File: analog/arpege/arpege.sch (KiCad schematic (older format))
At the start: 43 parts, among them J1 Conn_01x02, J2 Conn_01x02, J3 Conn_01x06, J4 AudioJack3, SW1 SW_SPDT, SW2 SW_SPDT, U1 TL062, U2 TL062

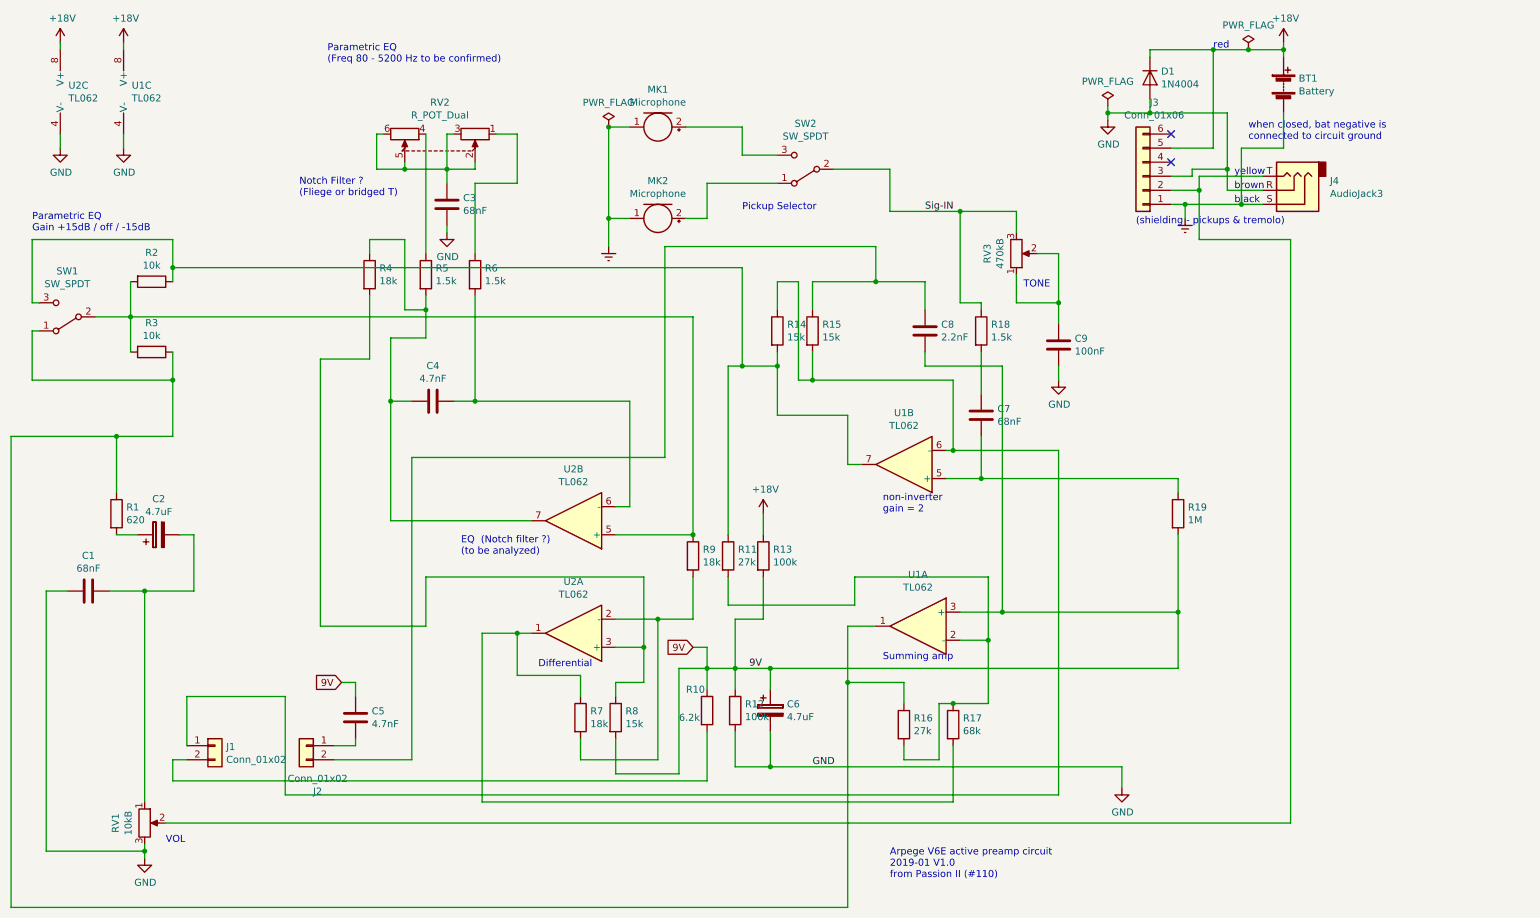
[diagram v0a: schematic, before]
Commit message: added some components values, clean up edge connector
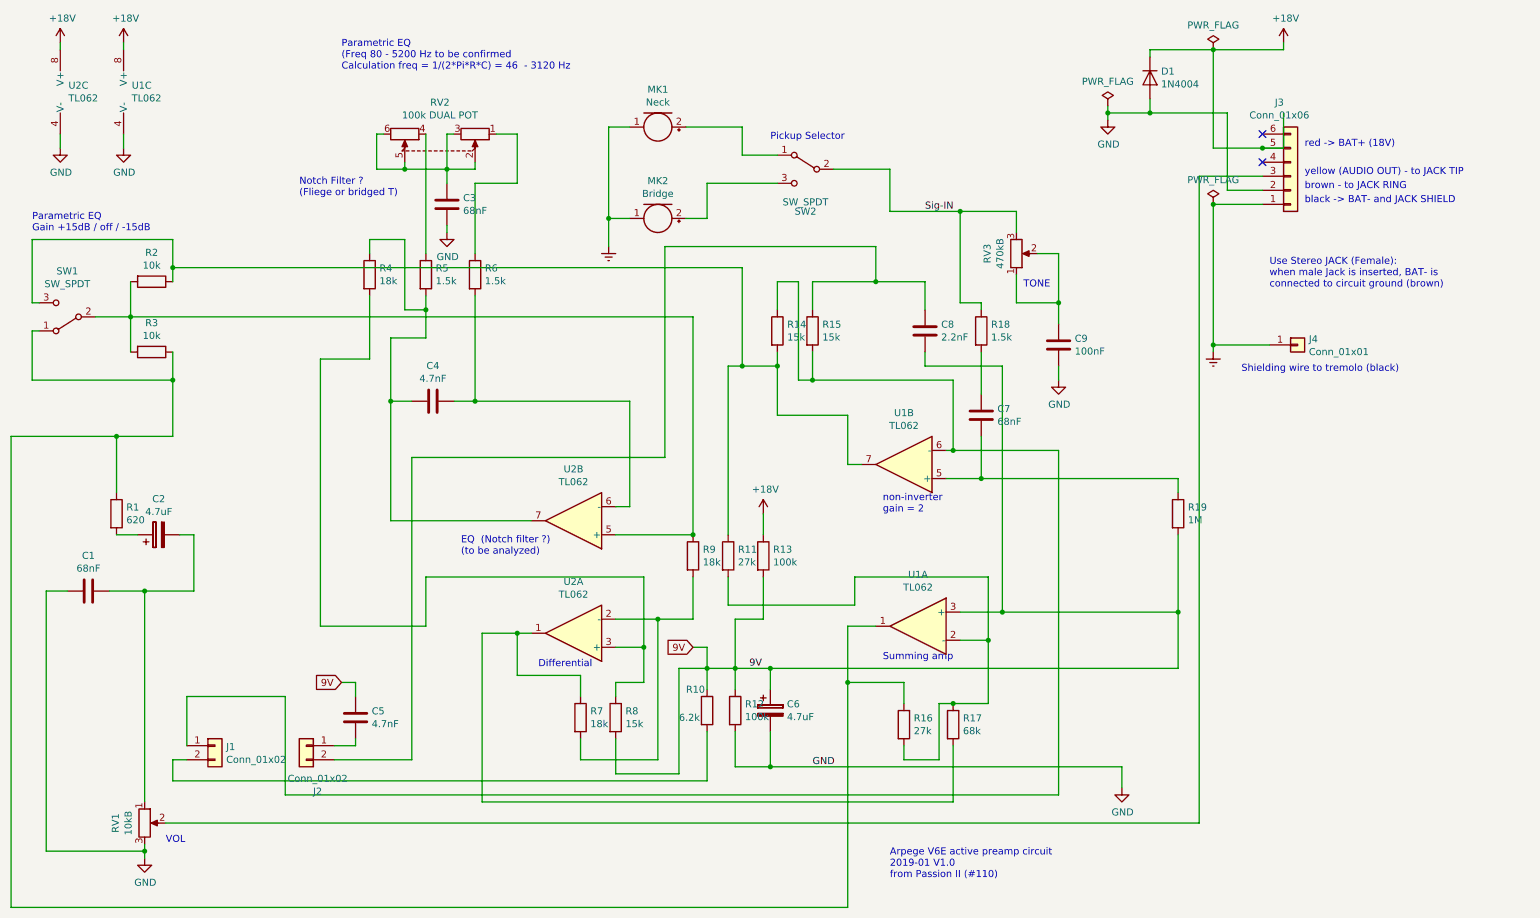
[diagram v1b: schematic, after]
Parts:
- removed BT1: Battery, symbol Device:Battery
- removed J4: AudioJack3, symbol Connector:AudioJack3
- added J4: Conn_01x01, symbol Connector_Generic:Conn_01x01
- MK1: value Microphone -> Neck
- MK2: value Microphone -> Bridge
- RV2: value R_POT_Dual -> 100k DUAL POT
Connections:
- net Earth: now also J4.1 (Pin_1)
- net GND: now also J3.2 (Pin_2); no longer J3.3 (Pin_3)
- net at RV1.2: now also J3.3 (Pin_3); no longer J3.2 (Pin_2)
- net at SW2.1 (A): now also MK1.2 (+); no longer MK2.2 (+)
- net at SW2.3 (C): now also MK2.2 (+); no longer MK1.2 (+)
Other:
- note added: "Parametric EQ \n(Freq 80 - 5200 Hz to be confirmed\nCalculation freq = 1/(2*Pi*R*C) = 46 - 3120 Hz"
- note added: "Shielding wire to tremolo (black)"
- note added: "Use Stereo JACK (Female): \nwhen male Jack is inserted, BAT- is \nconnected to circuit ground (brown)"
- note added: "black -> BAT- and JACK SHIELD"
- note added: "brown - to JACK RING"
- note added: "red -> BAT+ (18V)"
- note added: "yellow (AUDIO OUT) - to JACK TIP"
- note removed: "(shielding - pickups & tremolo)"
- note removed: "Parametric EQ \n(Freq 80 - 5200 Hz to be confirmed)"
- note removed: "black"
- note removed: "brown"
- note removed: "red"
- note removed: "when closed, bat negative is \nconnected to circuit ground"
- note removed: "yellow"
- moved on the sheet: J3
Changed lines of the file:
@@
 Arpege V6E active preamp circuit\n2019-01 V1.0\nfrom Passion II (#110)\n
-$Comp
-L Device:Battery BT1
-U 1 1 5C31AA7D
-P 9800 1150
-F 0 "BT1" H 9908 1196 50  0000 L CNN
-F 1 "Battery" H 9908 1105 50  0000 L CNN
-F 2 "" V 9800 1210 50  0001 C CNN
-F 3 "~" V 9800 1210 50  0001 C CNN
-	1    9800 1150
-	1    0    0    -1
-$EndComp
 $Comp
 L Device:R_POT RV3
@@
 	0    1    1    0
 $EndComp
-Wire Wire Line
-	9800 950  9800 900
 $Comp
 L arpege-rescue:+18V-power #PWR012
@@
 U 1 1 5C31D5B5
 P 6400 1750
-F 0 "SW2" H 6400 1425 50  0000 C CNN
+F 0 "SW2" H 6400 1450 50  0000 C CNN
 F 1 "SW_SPDT" H 6400 1516 50  0000 C CNN
 F 2 "" H 6400 1750 50  0001 C CNN
 F 3 "" H 6400 1750 50  0001 C CNN
 	1    6400 1750
-	-1   0    0    1
+	-1   0    0    -1
 $EndComp
 $Comp
@@
 P 3800 1600
 F 0 "RV2" H 3800 1275 50  0000 C CNN
-F 1 "R_POT_Dual" H 3800 1366 50  0000 C CNN
+F 1 "100k DUAL POT" H 3800 1366 50  0000 C CNN
 F 2 "" H 4050 1525 50  0001 C CNN
 F 3 "~" H 4050 1525 50  0001 C CNN
@@
 P 5350 1450
 F 0 "MK1" V 5083 1450 50  0000 C CNN
-F 1 "Microphone" V 5174 1450 50  0000 C CNN
+F 1 "Neck" V 5174 1450 50  0000 C CNN
 F 2 "" V 5350 1550 50  0001 C CNN
 F 3 "~" V 5350 1550 50  0001 C CNN
@@
 P 5350 2100
 F 0 "MK2" V 5083 2100 50  0000 C CNN
-F 1 "Microphone" V 5174 2100 50  0000 C CNN
+F 1 "Bridge" V 5174 2100 50  0000 C CNN
 F 2 "" V 5350 2200 50  0001 C CNN
 F 3 "~" V 5350 2200 50  0001 C CNN
 	1    5350 2100
 	0    1    1    0
-$EndComp
-$Comp
-L Connector:AudioJack3 J4
-U 1 1 5C31E95E
-P 9850 1900
-F 0 "J4" H 9570 1833 50  0000 R CNN
-F 1 "AudioJack3" H 9570 1924 50  0000 R CNN
-F 2 "" H 9850 1900 50  0001 C CNN
-F 3 "~" H 9850 1900 50  0001 C CNN
-	1    9850 1900
-	-1   0    0    1
 $EndComp
 $Comp
@@
 	1    0    0    -1
 $EndComp
-Text Notes 9450 1900 0    50   ~ 0
-brown
-Text Notes 9450 2000 0    50   ~ 0
-black
-Text Notes 9450 1800 0    50   ~ 0
-yellow
+Text Notes 9950 1900 0    50   ~ 0
+brown - to JACK RING
+Text Notes 9950 2000 0    50   ~ 0
+black -> BAT- and JACK SHIELD
+Text Notes 9950 1800 0    50   ~ 0
+yellow (AUDIO OUT) - to JACK TIP
 Wire Wire Line
 	9800 1350 9800 1600
 Wire Wire Line
-	9800 1600 9500 1600
-Wire Wire Line
-	9500 1600 9500 2000
-Wire Wire Line
-	9200 1800 9200 1900
+	9800 1600 9650 1600
 Wire Wire Line
 	9650 1900 9400 1900
-Wire Wire Line
-	9400 1750 9150 1750
-Wire Wire Line
-	9150 1750 9150 1800
-Wire Wire Line
-	9150 1800 9000 1800
 Wire Wire Line
 	9400 1350 8850 1350
@@
 L power:Earth #PWR011
 U 1 1 5C3212CD
-P 9100 2100
-F 0 "#PWR011" H 9100 1850 50  0001 C CNN
-F 1 "Earth" H 9100 1950 50  0001 C CNN
-F 2 "" H 9100 2100 50  0001 C CNN
-F 3 "~" H 9100 2100 50  0001 C CNN
-	1    9100 2100
-	1    0    0    -1
-$EndComp
-Wire Wire Line
-	9000 2000 9100 2000
-Wire Wire Line
-	9100 2000 9100 2100
-Text Notes 8750 2150 0    50   ~ 0
-(shielding - pickups & tremolo)
-Connection ~ 9100 2000
+P 9300 3050
+F 0 "#PWR011" H 9300 2800 50  0001 C CNN
+F 1 "Earth" H 9300 2900 50  0001 C CNN
+F 2 "" H 9300 3050 50  0001 C CNN
+F 3 "~" H 9300 3050 50  0001 C CNN
+	1    9300 3050
+	1    0    0    -1
+$EndComp
+Text Notes 9500 3200 0    50   ~ 0
+Shielding wire to tremolo (black)
 $Comp
 L power:GND #PWR09
@@
 	1550 1500 1550 1600
 Wire Wire Line
-	9800 900  9550 900
-Connection ~ 9800 900
-Wire Wire Line
 	9800 900  9800 850
-Text Notes 9300 900  0    50   ~ 0
-red
+Text Notes 9950 1600 0    50   ~ 0
+red -> BAT+ (18V)
 $Comp
 L power:PWR_FLAG #FLG02
 U 1 1 5C342F20
-P 9550 900
-F 0 "#FLG02" H 9550 975 50  0001 C CNN
-F 1 "PWR_FLAG" H 9550 1074 50  0000 C CNN
-F 2 "" H 9550 900 50  0001 C CNN
-F 3 "~" H 9550 900 50  0001 C CNN
-	1    9550 900
-	1    0    0    -1
-$EndComp
-Connection ~ 9550 900
-Wire Wire Line
-	9550 900  9300 900
+P 9300 900
+F 0 "#FLG02" H 9300 975 50  0001 C CNN
+F 1 "PWR_FLAG" H 9300 1074 50  0000 C CNN
+F 2 "" H 9300 900 50  0001 C CNN
+F 3 "~" H 9300 900 50  0001 C CNN
+	1    9300 900
+	1    0    0    -1
+$EndComp
 $Comp
 L power:PWR_FLAG #FLG01
@@
 L Connector_Generic:Conn_01x06 J3
 U 1 1 5C469EF8
-P 8800 1800
-F 0 "J3" H 8720 1275 50  0000 C CNN
-F 1 "Conn_01x06" H 8720 1366 50  0000 C CNN
-F 2 "" H 8800 1800 50  0001 C CNN
-F 3 "~" H 8800 1800 50  0001 C CNN
-	1    8800 1800
-	-1   0    0    1
+P 9850 1800
+F 0 "J3" H 9770 1275 50  0000 C CNN
+F 1 "Conn_01x06" H 9770 1366 50  0000 C CNN
+F 2 "" H 9850 1800 50  0001 C CNN
+F 3 "~" H 9850 1800 50  0001 C CNN
+	1    9850 1800
+	1    0    0    1
 $EndComp
 Wire Wire Line
 	9300 900  9300 1600
-Wire Wire Line
-	9300 1600 9000 1600
 Wire Wire Line
 	3600 3400 3450 3400
@@
 Wire Wire Line
 	1650 4350 1500 4350
-NoConn ~ 9000 1700
-NoConn ~ 9000 1500
+NoConn ~ 9650 1700
+NoConn ~ 9650 1500
 $Comp
 L Amplifier_Operational:TL062 U1
@@
 Sig-IN
 Wire Wire Line
-	9000 1900 9200 1900
-Wire Wire Line
 	1700 6650 1700 6600
 Wire Wire Line
@@
 L power:PWR_FLAG #FLG0101
 U 1 1 5CAD682B
-P 5000 1450
-F 0 "#FLG0101" H 5000 1525 50  0001 C CNN
-F 1 "PWR_FLAG" H 5000 1624 50  0000 C CNN
-F 2 "" H 5000 1450 50  0001 C CNN
-F 3 "~" H 5000 1450 50  0001 C CNN
-	1    5000 1450
-	1    0    0    -1
-$EndComp
-Connection ~ 5000 1450
-Text Notes 9550 1550 0    50   ~ 0
-when closed, bat negative is \nconnected to circuit ground
-Text Notes 3000 1000 0    50   ~ 0
-Parametric EQ \n(Freq 80 - 5200 Hz to be confirmed)
+P 9300 2000
+F 0 "#FLG0101" H 9300 2075 50  0001 C CNN
+F 1 "PWR_FLAG" H 9300 2174 50  0000 C CNN
+F 2 "" H 9300 2000 50  0001 C CNN
+F 3 "~" H 9300 2000 50  0001 C CNN
+	1    9300 2000
+	1    0    0    -1
+$EndComp
+Text Notes 9700 2600 0    50   ~ 0
+Use Stereo JACK (Female): \nwhen male Jack is inserted, BAT- is \nconnected to circuit ground (brown)
+Text Notes 3100 1050 0    50   ~ 0
+Parametric EQ \n(Freq 80 - 5200 Hz to be confirmed\nCalculation freq = 1/(2*Pi*R*C) = 46  - 3120 Hz
 Text Notes 900  2200 0    50   ~ 0
 Parametric EQ\nGain +15dB / off / -15dB
@@
 	1700 4750 2050 4750
 Wire Wire Line
-	9850 2250 9200 2250
-Wire Wire Line
-	9200 2250 9200 1900
-Connection ~ 9200 1900
-Wire Wire Line
 	1150 4750 1000 4750
 Wire Wire Line
@@
 Wire Wire Line
 	1700 6600 1700 6550
-Wire Wire Line
-	9100 2000 9500 2000
-Wire Wire Line
-	9400 1750 9400 1350
-Wire Wire Line
-	9400 1900 9400 1750
-Connection ~ 9400 1750
-Connection ~ 9500 2000
-Wire Wire Line
-	9500 2000 9650 2000
 Connection ~ 8550 1350
 Wire Wire Line
 	8550 1350 8550 1400
 Wire Wire Line
-	1850 6400 9850 6400
-Wire Wire Line
-	9850 2250 9850 6400
-Text Notes 5950 2050 0    50   ~ 0
+	1850 6400 9200 6400
+Text Notes 6150 1550 0    50   ~ 0
 Pickup Selector
+Wire Wire Line
+	9650 1600 9300 1600
+Connection ~ 9650 1600
+Wire Wire Line
+	9400 1350 9400 1900
+Wire Wire Line
+	9200 1800 9200 6400
+$Comp
+L Connector_Generic:Conn_01x01 J4
+U 1 1 5C5212B1
+P 9900 3000
+F 0 "J4" H 9980 3042 50  0000 L CNN
+F 1 "Conn_01x01" H 9980 2951 50  0000 L CNN
+F 2 "" H 9900 3000 50  0001 C CNN
+F 3 "~" H 9900 3000 50  0001 C CNN
+	1    9900 3000
+	1    0    0    -1
+$EndComp
+Wire Wire Line
+	9300 900  9800 900
+Wire Wire Line
+	9300 2000 9650 2000
+Wire Wire Line
+	9700 3000 9300 3000
+Wire Wire Line
+	9300 3000 9300 2000
+Connection ~ 9300 2000
+Wire Wire Line
+	9300 3050 9300 3000
+Connection ~ 9300 3000
 $EndSCHEMATC

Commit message: added notes / labels to booster switch signals
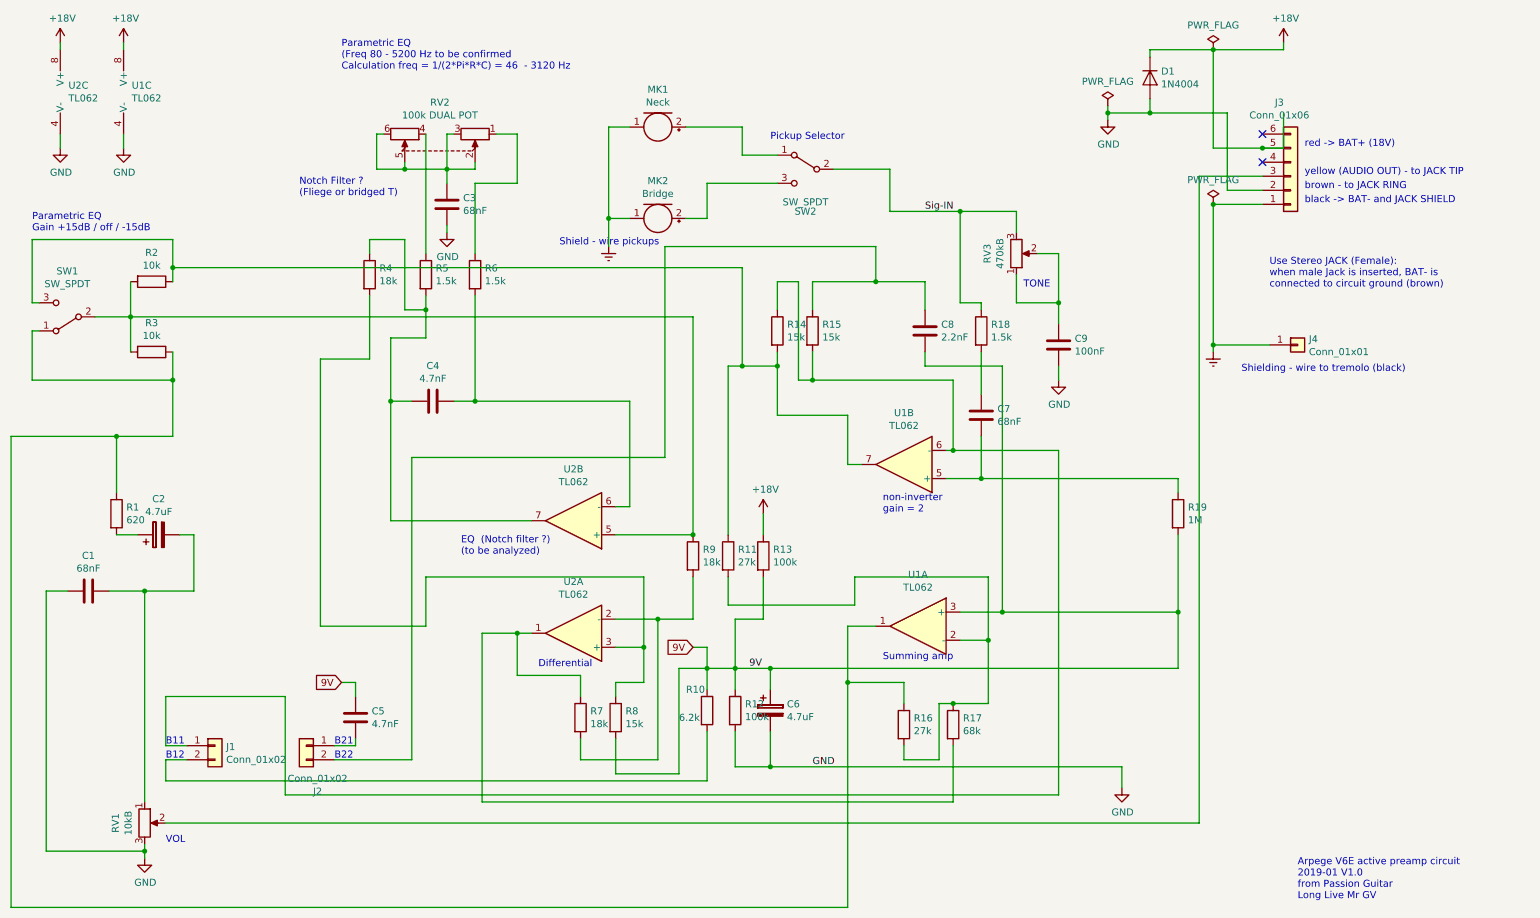
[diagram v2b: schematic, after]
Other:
- note added: "Arpege V6E active preamp circuit\n2019-01 V1.0\nfrom Passion Guitar\nLong Live Mr GV\n"
- note added: "B11"
- note added: "B12"
- note added: "B21"
- note added: "B22"
- note added: "Shield - wire pickups"
- note added: "Shielding - wire to tremolo (black)"
- note removed: "Arpege V6E active preamp circuit\n2019-01 V1.0\nfrom Passion II (#110)\n"
- note removed: "Shielding wire to tremolo (black)"
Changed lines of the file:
@@
 Comment4 ""
 $EndDescr
-Text Notes 7000 6800 0    50   ~ 0
-Arpege V6E active preamp circuit\n2019-01 V1.0\nfrom Passion II (#110)\n
+Text Notes 9900 6950 0    50   ~ 0
+Arpege V6E active preamp circuit\n2019-01 V1.0\nfrom Passion Guitar\nLong Live Mr GV\n
 $Comp
 L Device:R_POT RV3
@@
 $EndComp
 Text Notes 9500 3200 0    50   ~ 0
-Shielding wire to tremolo (black)
+Shielding - wire to tremolo (black)
 $Comp
 L power:GND #PWR09
@@
 	3700 1500 3700 2350
 Wire Wire Line
-	2000 5850 2000 5500
-Wire Wire Line
-	2000 5500 2700 5500
-Wire Wire Line
 	2700 5500 2700 6200
 Wire Wire Line
@@
 Connection ~ 7450 3750
 Wire Wire Line
-	2000 5950 1900 5950
-Wire Wire Line
-	1900 5950 1900 6100
-Wire Wire Line
-	1900 6100 5700 6100
+	2000 5950 1850 5950
+Wire Wire Line
+	1850 5950 1850 6100
+Wire Wire Line
+	1850 6100 5700 6100
 Wire Wire Line
 	5700 6100 5700 5750
@@
 	9300 3050 9300 3000
 Connection ~ 9300 3000
+Text Notes 4650 2300 0    50   ~ 0
+Shield - wire pickups
+Text Notes 1850 5850 0    50   ~ 0
+B11
+Text Notes 1850 5950 0    50   ~ 0
+B12
+Text Notes 3050 5850 0    50   ~ 0
+B21
+Text Notes 3050 5950 0    50   ~ 0
+B22
+Wire Wire Line
+	2000 5850 1850 5850
+Wire Wire Line
+	1850 5850 1850 5500
+Wire Wire Line
+	1850 5500 2700 5500
 $EndSCHEMATC

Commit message: updated POT values (EQ, tone)
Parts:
- RV2: value 100k DUAL POT -> 100k A Dual POT
- RV3: value 470kB -> 470kA
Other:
- note added: "Parametric EQ\n(Q factor or Gain ?)"
- note removed: "Parametric EQ\nGain +15dB / off / -15dB"
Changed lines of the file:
@@
 P 7900 2350
 F 0 "RV3" V 7693 2350 50  0000 C CNN
-F 1 "470kB" V 7784 2350 50  0000 C CNN
+F 1 "470kA" V 7784 2350 50  0000 C CNN
 F 2 "" H 7900 2350 50  0001 C CNN
 F 3 "~" H 7900 2350 50  0001 C CNN
@@
 P 3800 1600
 F 0 "RV2" H 3800 1275 50  0000 C CNN
-F 1 "100k DUAL POT" H 3800 1366 50  0000 C CNN
+F 1 "100k A Dual POT" H 3800 1366 50  0000 C CNN
 F 2 "" H 4050 1525 50  0001 C CNN
 F 3 "~" H 4050 1525 50  0001 C CNN
@@
 Parametric EQ \n(Freq 80 - 5200 Hz to be confirmed\nCalculation freq = 1/(2*Pi*R*C) = 46  - 3120 Hz
 Text Notes 900  2200 0    50   ~ 0
-Parametric EQ\nGain +15dB / off / -15dB
+Parametric EQ\n(Q factor or Gain ?)
 Wire Wire Line
 	1550 900  1550 850
